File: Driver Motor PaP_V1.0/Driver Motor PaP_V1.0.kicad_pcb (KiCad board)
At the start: 4 copper layers, 60 x 50 mm, 31 parts, among them J1 Conn_01x02, J2 Conn_01x02, J3 Conn_01x03, J4 Conn_01x05, J5 Conn_01x01, J6 Conn_01x02, J7 Conn_01x02, U1 LM358, U2 LM358, U3 LM358

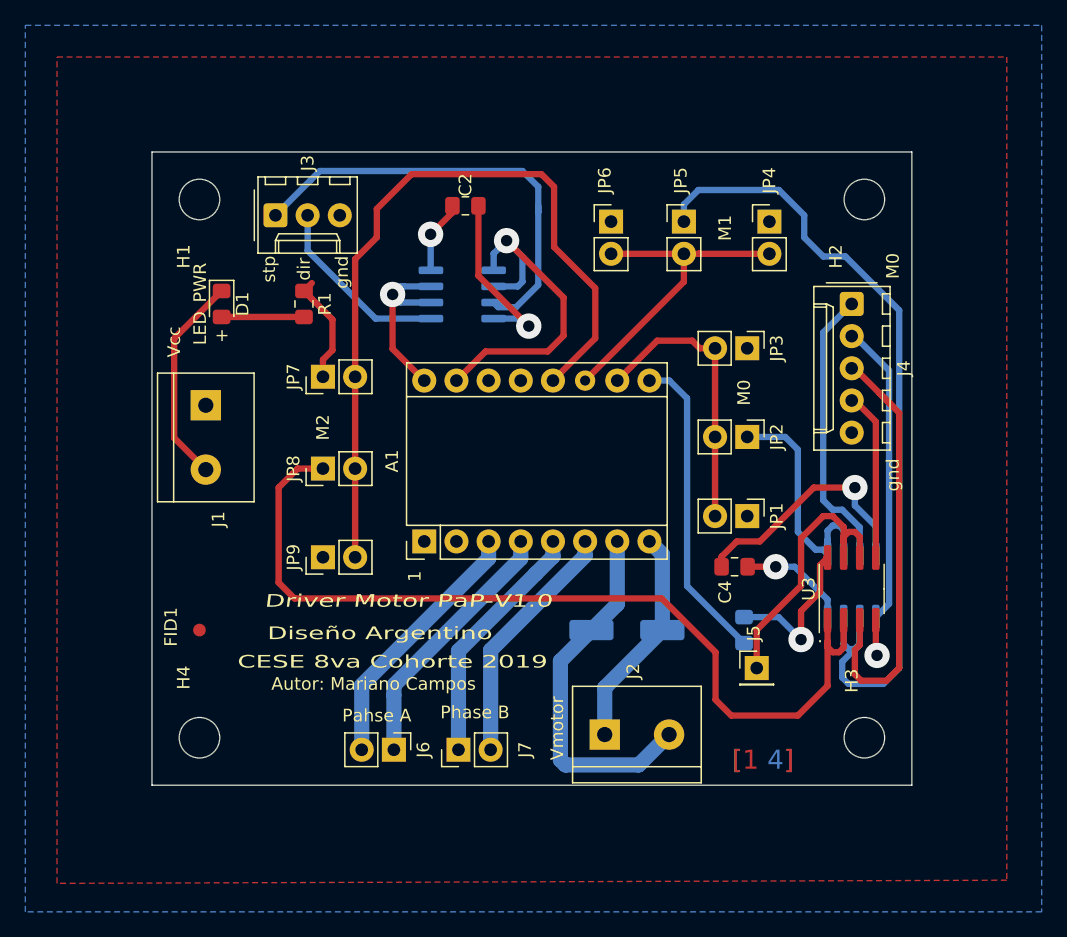
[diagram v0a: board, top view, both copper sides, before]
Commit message: modificación de margen y traslado de componentes a la capa superior
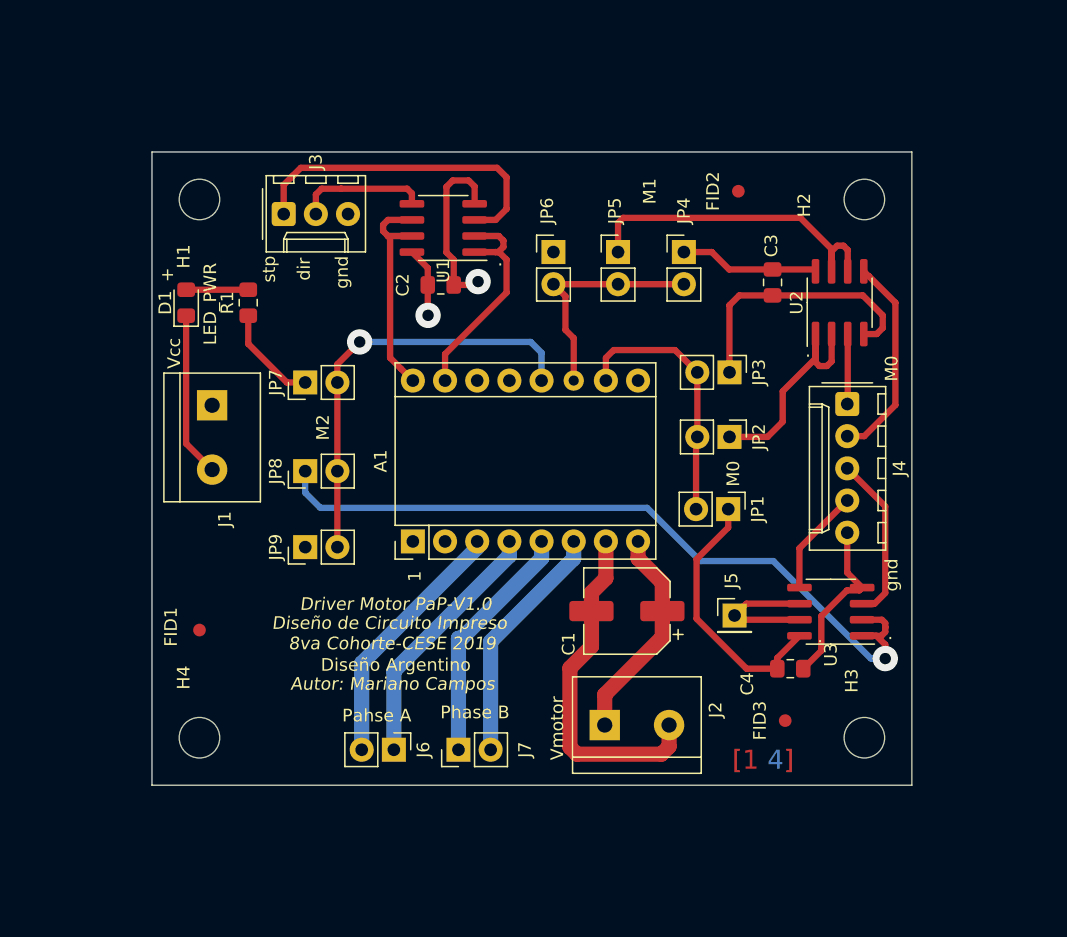
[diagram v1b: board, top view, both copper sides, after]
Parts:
- added FID2: Fiducial, Fiducial:Fiducial_1mm_Mask2mm, F.Cu at (153.8, 88.1)
- added FID3: Fiducial, Fiducial:Fiducial_1mm_Mask2mm, F.Cu at (157.5, 129.9)
- C1, C3, U1, U2: moved to F.Cu
- moved C3 27.5 mm to (156.5, 95.3)
- moved U2 22.4 mm to (161.8, 96.9), turned to 90 degrees
- moved C4 9.17 mm to (157.9, 125.8), turned to 0 degrees
- moved J4 7.91 mm to (162.4, 104.9)
- moved JP4 7.16 mm to (149.5, 92.9)
- moved C2 6.55 mm to (130.3, 95.5)
- moved JP5 5.73 mm to (144.3, 92.9)
- moved U1 5.46 mm to (130.5, 91.0)
- moved JP6 5.14 mm to (139.2, 92.9)
- moved J5 4.50 mm to (153.5, 121.6)
- moved R1 4.40 mm to (115.1, 96.9), turned to 90 degrees
- moved D1 2.80 mm to (110.2, 96.9), turned to 90 degrees
- moved U3 2.44 mm to (161.1, 121.3), turned to 180 degrees
- moved JP3 2.36 mm to (153.1, 102.4)
- moved JP9 1.61 mm to (119.6, 116.2)
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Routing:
- net Net-(JP5-Pad1): track 69.0 -> 27.0 mm
- net Net-(A1-Pad12): track 61.8 -> 33.8 mm, vias 0 -> 1
- net Net-(J4-Pad3): track 35.6 -> 13.3 mm
- net Net-(J4-Pad1): track 22.3 -> 5.54 mm
- net GND: track 78.0 -> 61.8 mm, vias 3 -> 1
- net Net-(J5-Pad1): track 22.3 -> 10.8 mm
- net Net-(JP8-Pad1): track 71.9 -> 60.8 mm, vias 0 -> 1
- net Net-(A1-Pad15): track 28.3 -> 18.1 mm, vias 1 -> 0
- net VCC: track 36.2 -> 45.6 mm, vias 3 -> 1
- net Net-(J3-Pad1): track 35.4 -> 26.4 mm
- net Net-(J4-Pad2): track 24.0 -> 16.4 mm
- net Net-(A1-Pad11): track 25.8 -> 18.6 mm
- net Net-(J4-Pad4): track 13.3 -> 8.44 mm
- net Net-(J3-Pad2): track 14.7 -> 10.3 mm
- net Net-(A1-Pad16): track 14.4 -> 17.6 mm, vias 1 -> 0
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- removed copper zone on B.Cu, net GND
- removed copper zone on F.Cu, net GND
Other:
- net class Default: clearance 0.25 -> 0.5
- rule trace_clearance: 0.25 -> 0.5
- board text added: "Diseño de Circuito Impreso 8va Cohorte-CESE 2019"
- board text added: "Mínimos (10 Mils Mayer ) Grillas: 0,25 mm. vías : 2mm ,agujeros 0,9 mm. Margen General: 0,5 mm. Ancho de pista : 0,5 mm y 1,2 mm. Distancia a borde: 0,5 mm. PCB espesor: 1,6mm. Terminación HASL. Se utilizo 4 capas a modo de ejercicio."
- board text removed: "CESE 8va Cohorte 2019"
- board text removed: "Mínimos (10 Mils Mayer ) Grillas: 0,25 mm. vías : 2mm ,agujeros 0,9 mm. Margen General: 0,25 mm. Ancho de pista : 0,5 mm y 1,2 mm. Distancia a borde: 0,5 mm. PCB espesor: 1,6mm. Terminación HASL."
